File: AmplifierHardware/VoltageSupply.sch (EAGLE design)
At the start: 28 parts, among them IC2 LT1074CT, IC3 7812TV, Q1 BC550B, Q3 IRF9530, Q5 MJE2955

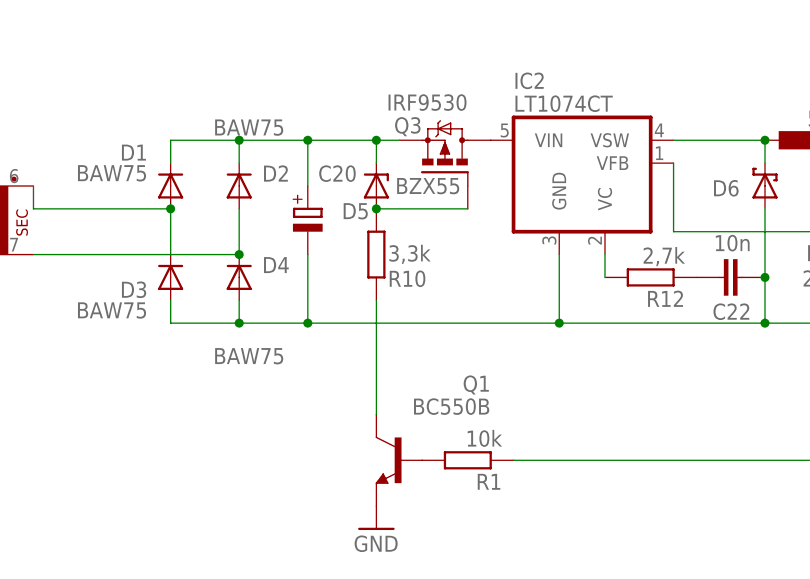
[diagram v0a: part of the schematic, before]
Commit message: Supply Voltage schematic adapted
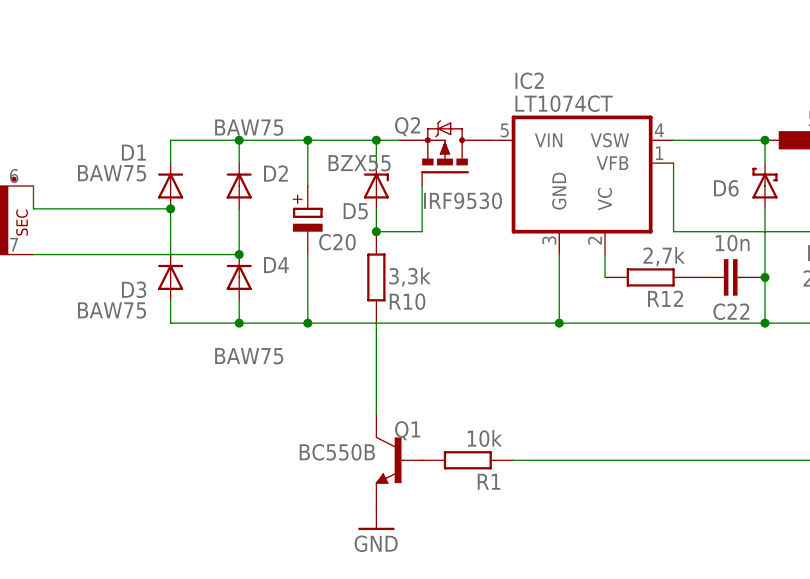
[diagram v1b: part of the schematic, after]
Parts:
- removed Q3: IRF9530, transistor-power:IRF9530
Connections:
- removed net N$30: IC2.VIN, Q3.D
- net N$31: no longer Q3.G
- net N$58: no longer Q3.S
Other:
- moved on the sheet: R10
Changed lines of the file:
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@@
 <part name="C20" library="rcl" deviceset="CPOL-EU" device="E5-10.5"/>
 <part name="IC2" library="linear-technology-3" deviceset="LT1074*" device="T" technology="C"/>
-<part name="Q3" library="transistor-power" deviceset="IRF9530" device=""/>
 <part name="D5" library="diode" deviceset="BZX55" device=""/>
 <part name="R10" library="rcl" deviceset="R-EU_" device="0207/2V" value="3,3k"/>
@@
 <part name="TR1" library="trafo" library_urn="urn:adsk.eagle:library:394" deviceset="EE20-1" device="" package3d_urn="urn:adsk.eagle:package:28342/1"/>
 <part name="SL2" library="con-amp-quick" library_urn="urn:adsk.eagle:library:125" deviceset="M02" device="" package3d_urn="urn:adsk.eagle:package:5956/1" value="220V"/>
+<part name="Q2" library="transistor-power" library_urn="urn:adsk.eagle:library:400" deviceset="P-MOSFET_SYMBOL" device="" value="IRF9530"/>
 </parts>
 <sheets>
@@
 </instance>
 <instance part="C20" gate="G$1" x="96.52" y="101.6" smashed="yes">
-<attribute name="NAME" x="97.663" y="104.6226" size="1.778" layer="95"/>
+<attribute name="NAME" x="97.663" y="97.0026" size="1.778" layer="95"/>
 <attribute name="VALUE" x="97.663" y="97.0026" size="1.778" layer="96"/>
 </instance>
@@
 <attribute name="VALUE" x="119.38" y="112.395" size="1.778" layer="96"/>
 </instance>
-<instance part="Q3" gate="G$1" x="111.76" y="106.68" smashed="yes" rot="R90">
-<attribute name="NAME" x="109.22" y="111.76" size="1.778" layer="95" rot="R180"/>
-<attribute name="VALUE" x="114.3" y="114.3" size="1.778" layer="96" rot="R180"/>
-</instance>
 <instance part="D5" gate="1" x="104.14" y="104.14" smashed="yes" rot="R90">
 <attribute name="NAME" x="103.378" y="102.235" size="1.778" layer="95" rot="R180"/>
-<attribute name="VALUE" x="113.538" y="105.029" size="1.778" layer="96" rot="R180"/>
-</instance>
-<instance part="R10" gate="G$1" x="104.14" y="96.52" smashed="yes" rot="R90">
-<attribute name="NAME" x="105.41" y="92.9386" size="1.778" layer="95"/>
-<attribute name="VALUE" x="105.41" y="95.758" size="1.778" layer="96"/>
+<attribute name="VALUE" x="105.918" y="107.569" size="1.778" layer="96" rot="R180"/>
+</instance>
+<instance part="R10" gate="G$1" x="104.14" y="93.98" smashed="yes" rot="R90">
+<attribute name="NAME" x="105.41" y="90.3986" size="1.778" layer="95"/>
+<attribute name="VALUE" x="105.41" y="93.218" size="1.778" layer="96"/>
 </instance>
 <instance part="C21" gate="G$1" x="165.1" y="99.06" smashed="yes">
@@
 </instance>
 <instance part="Q1" gate="G$1" x="106.68" y="73.66" smashed="yes" rot="MR0">
-<attribute name="NAME" x="116.84" y="81.28" size="1.778" layer="95" rot="MR0"/>
-<attribute name="VALUE" x="116.84" y="78.74" size="1.778" layer="96" rot="MR0"/>
+<attribute name="NAME" x="109.22" y="76.2" size="1.778" layer="95" rot="MR0"/>
+<attribute name="VALUE" x="104.14" y="73.66" size="1.778" layer="96" rot="MR0"/>
 </instance>
 <instance part="GND1" gate="1" x="208.28" y="86.36" smashed="yes">
@@
 <attribute name="VALUE" x="35.56" y="93.98" size="1.778" layer="96"/>
 <attribute name="NAME" x="35.56" y="104.902" size="1.778" layer="95"/>
+</instance>
+<instance part="Q2" gate="G$1" x="111.76" y="106.68" smashed="yes" rot="R90">
+<attribute name="NAME" x="109.22" y="111.76" size="1.778" layer="95" rot="R180"/>
+<attribute name="VALUE" x="109.22" y="101.6" size="1.778" layer="96"/>
 </instance>
 </instances>
@@
 <net name="N$31" class="0">
 <segment>
-<wire x1="104.14" y1="101.6" x2="114.3" y2="101.6" width="0.1524" layer="91"/>
-<junction x="104.14" y="101.6"/>
 <pinref part="D5" gate="1" pin="A"/>
-<pinref part="Q3" gate="G$1" pin="G"/>
 <pinref part="R10" gate="G$1" pin="2"/>
+<wire x1="104.14" y1="99.06" x2="104.14" y2="101.6" width="0.1524" layer="91"/>
+<wire x1="109.22" y1="104.14" x2="109.22" y2="99.06" width="0.1524" layer="91"/>
+<wire x1="109.22" y1="99.06" x2="104.14" y2="99.06" width="0.1524" layer="91"/>
+<junction x="104.14" y="99.06"/>
 </segment>
 </net>
@@
 <segment>
 <pinref part="R10" gate="G$1" pin="1"/>
-<wire x1="104.14" y1="91.44" x2="104.14" y2="78.74" width="0.1524" layer="91"/>
 <pinref part="Q1" gate="G$1" pin="C"/>
+<wire x1="104.14" y1="88.9" x2="104.14" y2="78.74" width="0.1524" layer="91"/>
 </segment>
 </net>
@@
 <pinref part="D6" gate="G$1" pin="C"/>
 <pinref part="L1" gate="G$1" pin="1"/>
-</segment>
-</net>
-<net name="N$30" class="0">
-<segment>
-<pinref part="IC2" gate="G$1" pin="VIN"/>
-<pinref part="Q3" gate="G$1" pin="D"/>
 </segment>
 </net>
@@
 <junction x="88.9" y="109.22"/>
 <pinref part="D5" gate="1" pin="C"/>
-<pinref part="Q3" gate="G$1" pin="S"/>
 <pinref part="C20" gate="G$1" pin="+"/>
 <pinref part="D2" gate="D" pin="C"/>
